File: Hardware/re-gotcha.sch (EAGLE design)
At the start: 1 part, among them U1 DA14580-01A32

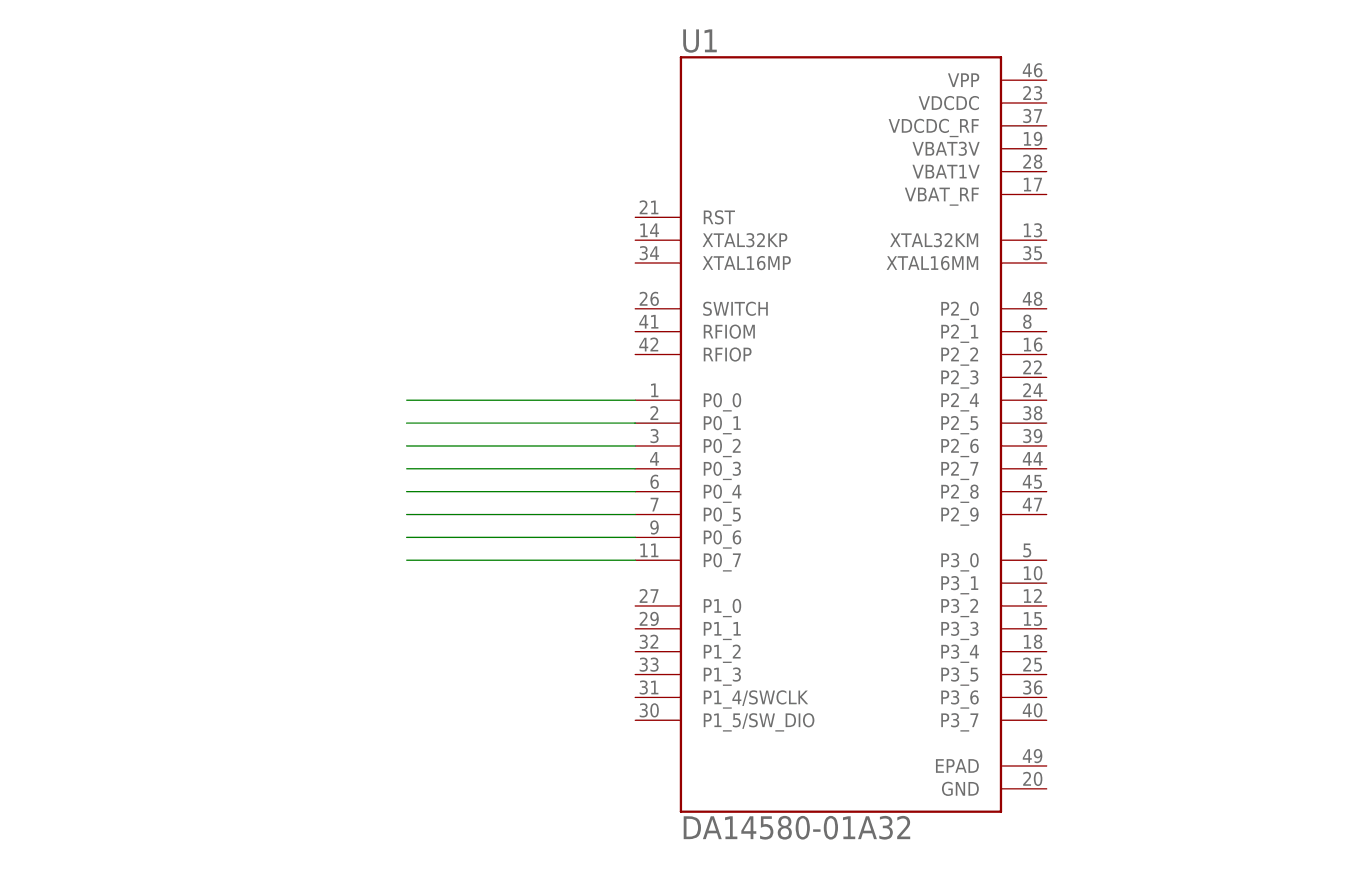
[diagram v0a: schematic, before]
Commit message: Founf LTC1517 onboard.
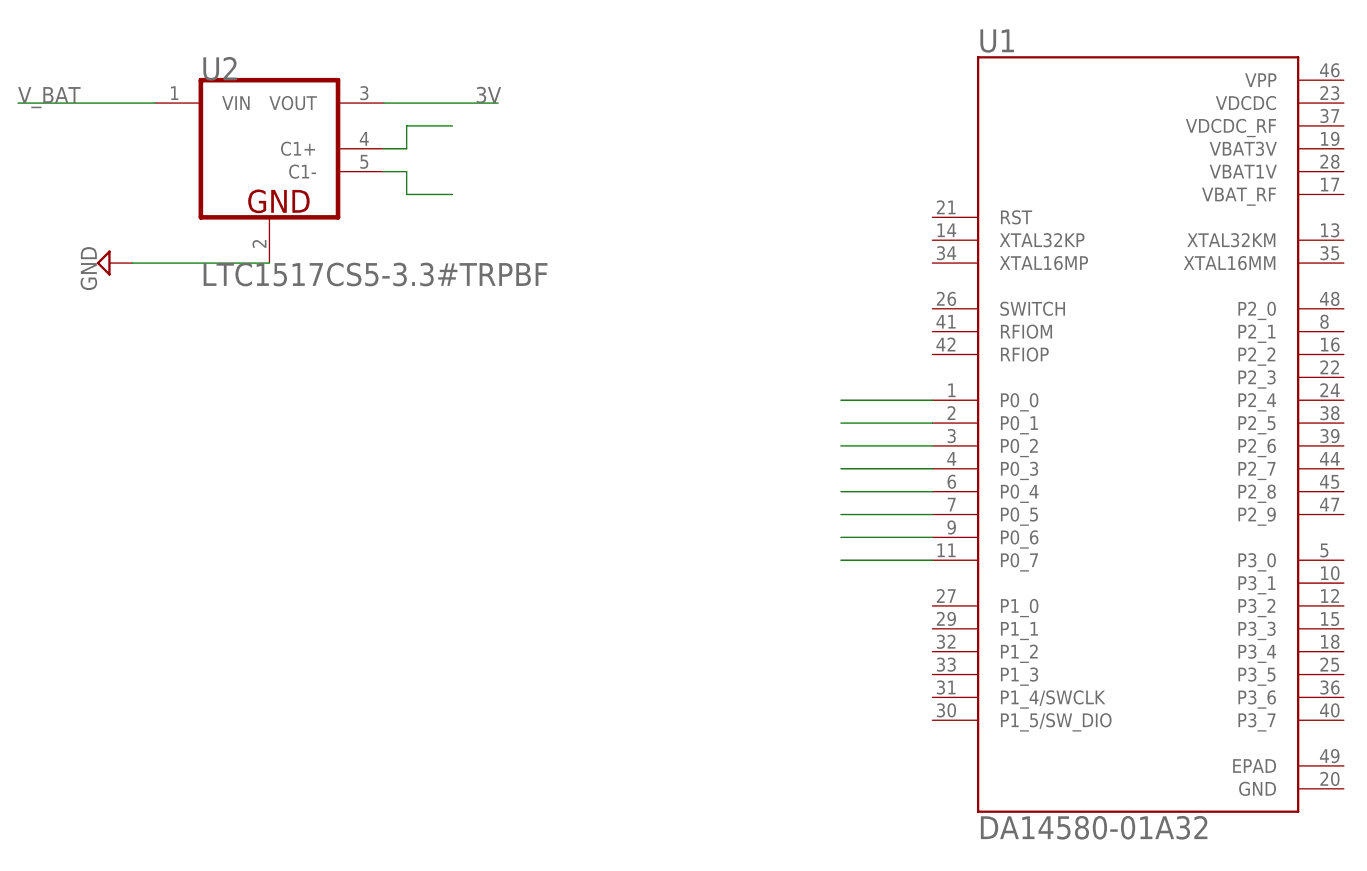
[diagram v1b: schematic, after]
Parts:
- added U2: LINEAR_TECHNOLOGY_LTC1517CS5-3.3#TRPBFLINEAR_TECHNOLOGY_LTC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, Linear Technology - LTC1517CS5-3.3#TRPBF:LINEAR_TECHNOLOGY_LTC1517CS5-3.3#TRPBFLINEAR_TECHNOLOGY_LTC1517CS5-3.3#TRPBF_0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
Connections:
- new net 3V: U2.VOUT
- new net GND: U2.GND
- new net N$10: U2.C1-
- new net N$9: U2.C1+
- new net V_BAT: U2.VIN
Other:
- moved on the sheet: U1

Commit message: Update
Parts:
- added 233DH: MCP4725, SparkFun-IC-Conversion:MCP4725SOT-23
- added 65Z5: LM50, linear:LM50
- added AKAA: (no value), transistor:MMBTA64LT1-PNP_DARL-SOT23-BEC
- added C1: (no value), adafruit:C-USC1206
- added Y1: 16MHz, SparkFun-Clocks:CRYSTAL-16MHZSMD-5X3.2
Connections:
- new net TOG: 233DH.AO
- new net TOUCH: 233DH.VOUT, C1.2
- net 3V: now also 233DH.SCL
- net GND: now also 233DH.VSS, AKAA.C, C1.1
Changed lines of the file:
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@@
 <part name="U2" library="Linear Technology - LTC1517CS5-3.3#TRPBF" deviceset="LINEAR_TECHNOLOGY_LTC1517CS5-3.3#TRPBF" device="LINEAR_TECHNOLOGY_LTC1517CS5-3.3#TRPBF_0_1"/>
 <part name="SUPPLY1" library="supply2" library_urn="urn:adsk.eagle:library:372" deviceset="GND" device=""/>
+<part name="233DH" library="SparkFun-IC-Conversion" deviceset="MCP4725" device="SOT-23" value="MCP4725"/>
+<part name="C1" library="adafruit" library_urn="urn:adsk.eagle:library:420" deviceset="C-US" device="C1206" package3d_urn="urn:adsk.eagle:package:6240335/1"/>
+<part name="65Z5" library="linear" library_urn="urn:adsk.eagle:library:262" deviceset="LM50" device="" package3d_urn="urn:adsk.eagle:package:16489/2"/>
+<part name="AKAA" library="transistor" library_urn="urn:adsk.eagle:library:402" deviceset="*-PNP_DARL-" device="SOT23-BEC" package3d_urn="urn:adsk.eagle:package:28748/2" technology="MMBTA64LT1"/>
+<part name="Y1" library="SparkFun-Clocks" deviceset="CRYSTAL-16MHZ" device="SMD-5X3.2" value="16MHz"/>
 </parts>
 <sheets>
@@
 <instance part="SUPPLY1" gate="GND" x="-20.32" y="73.66" smashed="yes" rot="R270">
 <attribute name="VALUE" x="-23.495" y="75.565" size="1.778" layer="96" rot="R270"/>
+</instance>
+<instance part="233DH" gate="U1" x="-2.54" y="53.34" smashed="yes">
+<attribute name="NAME" x="-10.16" y="59.182" size="1.778" layer="95"/>
+<attribute name="VALUE" x="-10.16" y="45.72" size="1.778" layer="96"/>
+</instance>
+<instance part="C1" gate="G$1" x="-20.32" y="63.5" smashed="yes">
+<attribute name="NAME" x="-19.304" y="64.135" size="1.778" layer="95"/>
+<attribute name="VALUE" x="-19.304" y="59.309" size="1.778" layer="96"/>
+</instance>
+<instance part="65Z5" gate="G$1" x="7.62" y="27.94" smashed="yes">
+<attribute name="NAME" x="0" y="31.75" size="1.778" layer="95"/>
+<attribute name="VALUE" x="10.16" y="20.32" size="1.778" layer="96"/>
+</instance>
+<instance part="AKAA" gate="G$1" x="-35.56" y="33.02" smashed="yes">
+<attribute name="NAME" x="-43.18" y="40.64" size="1.778" layer="95"/>
+<attribute name="VALUE" x="-43.18" y="38.1" size="1.778" layer="96"/>
+</instance>
+<instance part="Y1" gate="G$1" x="-15.24" y="2.54" smashed="yes">
+<attribute name="NAME" x="-15.24" y="4.572" size="1.778" layer="95" font="vector" align="bottom-center"/>
+<attribute name="VALUE" x="-15.24" y="0.508" size="1.778" layer="96" font="vector" align="top-center"/>
 </instance>
 </instances>
@@
 <segment>
 <pinref part="U2" gate="G$0" pin="VOUT"/>
-<wire x1="10.16" y1="91.44" x2="22.86" y2="91.44" width="0.1524" layer="91"/>
+<wire x1="10.16" y1="91.44" x2="33.02" y2="91.44" width="0.1524" layer="91"/>
 <label x="20.32" y="91.44" size="1.778" layer="95"/>
+<pinref part="233DH" gate="U1" pin="SCL"/>
+<wire x1="7.62" y1="53.34" x2="33.02" y2="53.34" width="0.1524" layer="91"/>
+<wire x1="33.02" y1="53.34" x2="33.02" y2="91.44" width="0.1524" layer="91"/>
 </segment>
 </net>
@@
 <wire x1="-2.54" y1="73.66" x2="-17.78" y2="73.66" width="0.1524" layer="91"/>
 <pinref part="SUPPLY1" gate="GND" pin="GND"/>
+<wire x1="-17.78" y1="73.66" x2="-17.78" y2="68.58" width="0.1524" layer="91"/>
+<junction x="-17.78" y="73.66"/>
+<wire x1="-17.78" y1="68.58" x2="-20.32" y2="68.58" width="0.1524" layer="91"/>
+<pinref part="233DH" gate="U1" pin="VSS"/>
+<wire x1="-20.32" y1="68.58" x2="-38.1" y2="68.58" width="0.1524" layer="91"/>
+<wire x1="-12.7" y1="53.34" x2="-38.1" y2="53.34" width="0.1524" layer="91"/>
+<wire x1="-38.1" y1="68.58" x2="-38.1" y2="63.5" width="0.1524" layer="91"/>
+<pinref part="C1" gate="G$1" pin="1"/>
+<wire x1="-38.1" y1="63.5" x2="-38.1" y2="53.34" width="0.1524" layer="91"/>
+<wire x1="-20.32" y1="66.04" x2="-20.32" y2="68.58" width="0.1524" layer="91"/>
+<junction x="-20.32" y="68.58"/>
+<pinref part="AKAA" gate="G$1" pin="C"/>
+<wire x1="-30.48" y1="27.94" x2="-30.48" y2="22.86" width="0.1524" layer="91"/>
+<wire x1="-30.48" y1="22.86" x2="-50.8" y2="22.86" width="0.1524" layer="91"/>
+<wire x1="-50.8" y1="22.86" x2="-50.8" y2="63.5" width="0.1524" layer="91"/>
+<wire x1="-50.8" y1="63.5" x2="-38.1" y2="63.5" width="0.1524" layer="91"/>
+<junction x="-38.1" y="63.5"/>
+</segment>
+</net>
+<net name="TOUCH" class="0">
+<segment>
+<pinref part="233DH" gate="U1" pin="VOUT"/>
+<wire x1="-12.7" y1="55.88" x2="-20.32" y2="55.88" width="0.1524" layer="91"/>
+<label x="-33.02" y="55.88" size="1.778" layer="95"/>
+<pinref part="C1" gate="G$1" pin="2"/>
+<wire x1="-20.32" y1="55.88" x2="-33.02" y2="55.88" width="0.1524" layer="91"/>
+<wire x1="-20.32" y1="58.42" x2="-20.32" y2="55.88" width="0.1524" layer="91"/>
+<junction x="-20.32" y="55.88"/>
+</segment>
+</net>
+<net name="TOG" class="0">
+<segment>
+<pinref part="233DH" gate="U1" pin="AO"/>
+<wire x1="7.62" y1="55.88" x2="7.62" y2="58.42" width="0.1524" layer="91"/>
+<wire x1="7.62" y1="58.42" x2="20.32" y2="58.42" width="0.1524" layer="91"/>
+<label x="15.24" y="58.42" size="1.778" layer="95"/>
 </segment>
 </net>
@@
 will not be understood (or retained) with this version.
 </note>
+<note version="8.3" severity="warning">
+Since Version 8.3, EAGLE supports the association of 3D packages
+with devices in libraries, schematics, and board files. Those 3D
+packages will not be understood (or retained) with this version.
+</note>
 </compatibility>

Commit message: updates
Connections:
- new net 16MM: U1.XTAL16MM, Y1.1
- new net 16MP: U1.XTAL16MP, Y1.2
- new net RF_GND: U1.RFIOM
- new net RF_INOUT: U1.RFIOP
- new net VBAT3V: U1.VBAT3V, U1.VBAT_RF
- new net VDCDC: U1.VDCDC, U1.VDCDC_RF
- net GND: now also U1.VBAT1V
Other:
- note added: "RESET is Active HIGH"
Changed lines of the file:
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@@
 <?xml version="1.0" encoding="utf-8"?>
 <!DOCTYPE eagle SYSTEM "eagle.dtd">
-<eagle version="9.5.2">
+<eagle version="9.6.2">
 <drawing>
 <settings>
@@
 <sheet>
 <plain>
+<text x="55.88" y="114.3" size="1.778" layer="97">RESET is Active HIGH</text>
 </plain>
 <instances>
@@
 <junction x="-38.1" y="63.5"/>
 </segment>
+<segment>
+<pinref part="U1" gate="G$1" pin="VBAT1V"/>
+<wire x1="116.84" y1="83.82" x2="121.92" y2="83.82" width="0.1524" layer="91"/>
+<label x="116.84" y="83.82" size="1.778" layer="95"/>
+</segment>
 </net>
 <net name="TOUCH" class="0">
@@
 </segment>
 </net>
+<net name="16MM" class="0">
+<segment>
+<pinref part="Y1" gate="G$1" pin="1"/>
+<wire x1="-17.78" y1="2.54" x2="-30.48" y2="2.54" width="0.1524" layer="91"/>
+<label x="-30.48" y="2.54" size="1.778" layer="95"/>
+</segment>
+<segment>
+<pinref part="U1" gate="G$1" pin="XTAL16MM"/>
+<wire x1="116.84" y1="73.66" x2="129.54" y2="73.66" width="0.1524" layer="91"/>
+<label x="124.46" y="73.66" size="1.778" layer="95"/>
+</segment>
+</net>
+<net name="16MP" class="0">
+<segment>
+<pinref part="Y1" gate="G$1" pin="2"/>
+<wire x1="-12.7" y1="2.54" x2="7.62" y2="2.54" width="0.1524" layer="91"/>
+<wire x1="10.16" y1="2.54" x2="7.62" y2="2.54" width="0.1524" layer="91"/>
+<label x="5.08" y="2.54" size="1.778" layer="95"/>
+</segment>
+<segment>
+<pinref part="U1" gate="G$1" pin="XTAL16MP"/>
+<wire x1="71.12" y1="73.66" x2="60.96" y2="73.66" width="0.1524" layer="91"/>
+<label x="60.96" y="73.66" size="1.778" layer="95"/>
+</segment>
+</net>
+<net name="VBAT3V" class="0">
+<segment>
+<pinref part="U1" gate="G$1" pin="VBAT_RF"/>
+<wire x1="116.84" y1="81.28" x2="127" y2="81.28" width="0.1524" layer="91"/>
+<wire x1="127" y1="81.28" x2="127" y2="86.36" width="0.1524" layer="91"/>
+<pinref part="U1" gate="G$1" pin="VBAT3V"/>
+<wire x1="127" y1="86.36" x2="116.84" y2="86.36" width="0.1524" layer="91"/>
+<label x="121.92" y="86.36" size="1.778" layer="95"/>
+</segment>
+</net>
+<net name="VDCDC" class="0">
+<segment>
+<pinref part="U1" gate="G$1" pin="VDCDC"/>
+<wire x1="116.84" y1="91.44" x2="134.62" y2="91.44" width="0.1524" layer="91"/>
+<wire x1="134.62" y1="91.44" x2="134.62" y2="88.9" width="0.1524" layer="91"/>
+<pinref part="U1" gate="G$1" pin="VDCDC_RF"/>
+<wire x1="134.62" y1="88.9" x2="116.84" y2="88.9" width="0.1524" layer="91"/>
+<label x="127" y="91.44" size="1.778" layer="95"/>
+</segment>
+</net>
+<net name="RF_INOUT" class="0">
+<segment>
+<pinref part="U1" gate="G$1" pin="RFIOP"/>
+<wire x1="71.12" y1="63.5" x2="60.96" y2="63.5" width="0.1524" layer="91"/>
+<label x="58.42" y="63.5" size="1.778" layer="95"/>
+</segment>
+</net>
+<net name="RF_GND" class="0">
+<segment>
+<pinref part="U1" gate="G$1" pin="RFIOM"/>
+<wire x1="71.12" y1="66.04" x2="60.96" y2="66.04" width="0.1524" layer="91"/>
+<label x="60.96" y="66.04" size="1.778" layer="95"/>
+</segment>
+</net>

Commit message: Update
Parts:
- removed U1: DA14580-01A32, DA14580-01A32:DA14580-01A32
- added 5F2A75JQG1: 25C040ST, microchip:25C040ST
- added C2, C3, C4, C5: (no value), adafruit:C-US025-024X044
- added R1, R2, R3: (no value), adafruit:R-US_0204/2V
- added U$1: DA14580, brandonsmith:DA14580
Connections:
- removed net N$2: U1.P0_1
- removed net N$3: U1.P0_2
- removed net N$4: U1.P0_3
- removed net N$5: U1.P0_5
- removed net N$6: U1.P0_4
- removed net N$7: U1.P0_7
- removed net N$8: U1.P0_6
- removed net RF_GND: U1.RFIOM
- removed net RF_INOUT: U1.RFIOP
- removed net VBAT3V: U1.VBAT3V, U1.VBAT_RF
- removed net VDCDC: U1.VDCDC, U1.VDCDC_RF
- new net N$11: R1.2, U$1.P2_2
- new net N$12: C3.2, C4.2, U$1.VBAT3V, U$1.VBAT_RF
- new net N$13: R2.2, U$1.SWITCH
- new net SCK: 5F2A75JQG1.SCK
- new net SDI: 5F2A75JQG1.SI
- new net SDO: 5F2A75JQG1.SO
- new net VCCDC: C2.2, C5.2, R2.1, U$1.VCCDC, U$1.VDCDC_RF
- new net VIN: 65Z5.GND
- new net VOUT: 5F2A75JQG1.VCC, 65Z5.+VS
- new net WP_TRY: R3.2, U$1.P0_3
- net 16MM: now also U$1.XTAL16MM; no longer U1.XTAL16MM
- net 16MP: now also U$1.XTAL16MP; no longer U1.XTAL16MP
- net GND: now also 5F2A75JQG1.GND, 65Z5.VO, C2.1, C3.1, C4.1, C5.1, U$1.VBAT_1V; no longer U1.VBAT1V
- net N$1: now also 5F2A75JQG1.!WP, R3.1; no longer U1.P0_0
- net TOUCH: now also R1.1

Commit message: Updates
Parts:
- removed 233DH: MCP4725, SparkFun-IC-Conversion:MCP4725SOT-23
- removed R2: (no value), adafruit:R-US_0204/2V
- added 1N: 500mA/300V, SparkFun-DiscreteSemi:TRANS_NPN-MMBTA42
- added A1: 2.45GHz, SparkFun-RF:ANTENNA2.4GHZ-6.5X2.2MM
- added JP1: (no value), adafruit:PINHD-1X14
- added L1: (no value), BeagleBone_Blue_R3:INDUCTOR
- added U$2: 233DH, brandonsmith:233DH
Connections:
- new net CS: 5F2A75JQG1.!CS, R3.1, U$1.P0_3
- new net N$2: C1.2, U$2.Q
- new net SCL: JP1.10, U$1.P2_0
- new net SDA: JP1.11, U$1.P2_1
- new net VCC_D: JP1.14
- net 3V: now also U$2.AHLB, U$2.VDD; no longer 233DH.SCL
- net GND: now also U$1.RFIOM, U$2.VSS; no longer 233DH.VSS
- net N$1: now also A1.SIGNAL, U$1.RFIOP; no longer 5F2A75JQG1.!WP, R3.1
- net N$13: now also L1.1; no longer R2.2
- net SCK: now also U$1.P0_0
- net SDI: now also U$1.P0_6
- net SDO: now also U$1.P0_5
- net TOG: now also U$2.TOG; no longer 233DH.AO
- net TOUCH: no longer 233DH.VOUT, C1.2
- net VCCDC: now also L1.2; no longer R2.1
- net WP_TRY: now also 5F2A75JQG1.!HOLD, 5F2A75JQG1.!WP; no longer U$1.P0_3
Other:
- note added: "RX"
- note added: "TX"
- moved on the sheet: C1, R3
